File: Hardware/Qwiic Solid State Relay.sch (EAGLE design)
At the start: 42 parts, among them J2 Qwiic Right Angle, J3 Qwiic Right Angle, J9 AVR_SPI_PROG_3X2TESTPOINTS, K1 25A Solid State Relay, K2 25A Solid State Relay, Q1 600mA/40V, Q2 600mA/40V, U4 ATTINY84-ARDUINO

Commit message: post review/checklist changes
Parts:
- added D3, D4: (no value), SparkFun-LED:LED5MM
- added J6: (no value), SparkFun-Connectors:CONN_01PTH_NO_SILK_YES_STOP
- added JP10, JP3, JP8: STAND-OFF, SparkFun-Hardware:STAND-OFF
- added LOGO4: QWIIC_LOGO_5MM, SparkFun-Aesthetics:QWIIC_LOGO_5MM
- added R7, R8: 1k, SparkFun-Resistors:1KOHM-0603-1/10W-1%
- ADR, PWR: value JUMPER-SMT_2_NO_SILK -> JUMPER-SMT_2_NC_TRACE_SILK; device SparkFun-Jumpers:JUMPER-SMT_2_NO_SILK -> SparkFun-Jumpers:JUMPER-SMT_2_NC_TRACE_SILK
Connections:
- removed net N$1: D2.C, Q2.C, R5.1
- removed net N$2: D1.C, Q1.C, R2.1
- removed net RELAY_CTRL3: U4.(A1)1
- removed net RELAY_CTRL4: U4.(A0)0
- new net N$11: D1.C, D3.C, Q1.C, R2.1
- new net N$12: D3.A, R7.1
- new net N$17: D2.C, D4.C, Q2.C, R5.1
- new net N$18: D4.A, R8.1
- net !RESET: now also J6.1
- net 3.3V: now also R7.2, R8.2
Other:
- note added: "VIN: 2.7-5.5V"

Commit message: adding panel
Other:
- note added: "Address 0x6D: HIGH (Open Jumper) Address 0x6C: LOW (Default)"
- note removed: "Address 0x6D: HIGH (Default) Address 0x6C: LOW (Close Jumper)"
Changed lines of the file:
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@@
 <text x="149.86" y="114.3" size="2.54" layer="94" font="vector">ATtiny84</text>
 <text x="63.5" y="114.3" size="2.54" layer="94" font="vector">Programming Header</text>
-<text x="101.6" y="2.54" size="1.27" layer="97" font="vector">Address 0x6D: HIGH (Default)
-Address 0x6C: LOW (Close Jumper)</text>
+<text x="101.6" y="2.54" size="1.27" layer="97" font="vector">Address 0x6D: HIGH (Open Jumper)
+Address 0x6C: LOW (Default)</text>
 <wire x1="119.38" y1="12.7" x2="119.38" y2="7.62" width="0.2032" layer="97" style="dashdot"/>
 <text x="115.824" y="24.638" size="1.27" layer="97" font="vector">Cut jumper

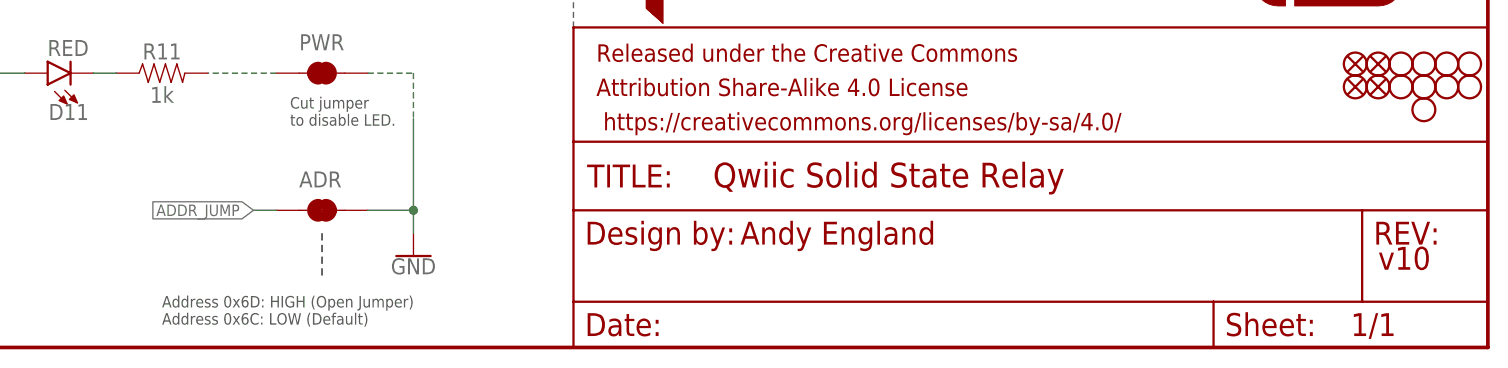
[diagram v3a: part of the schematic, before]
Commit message: updating address note
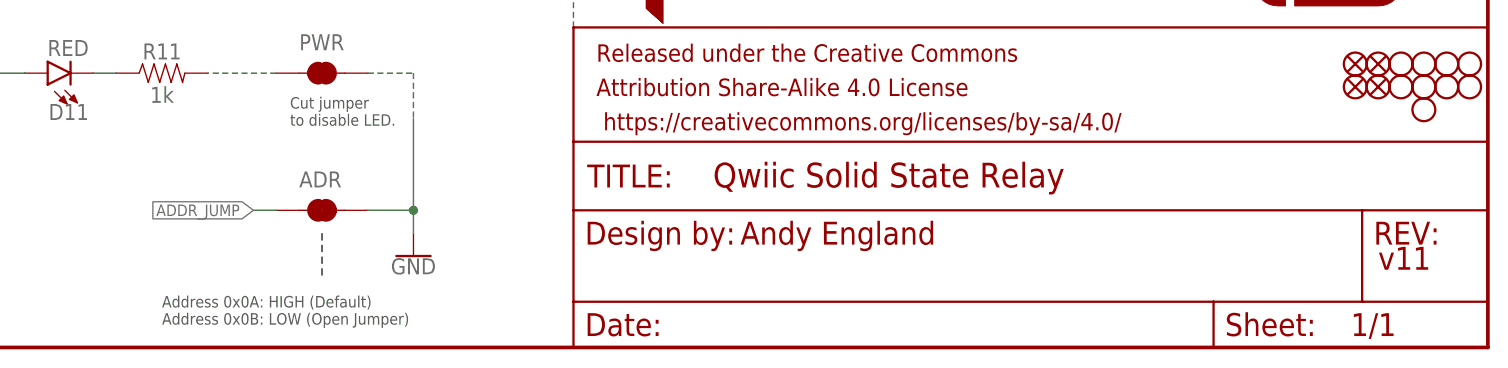
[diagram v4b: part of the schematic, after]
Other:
- note added: "Address 0x0A: HIGH (Default) Address 0x0B: LOW (Open Jumper)"
- note added: "v11"
- note removed: "Address 0x6D: HIGH (Open Jumper) Address 0x6C: LOW (Default)"
- note removed: "v10"
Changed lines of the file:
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@@
 <plain>
 <text x="165.862" y="11.43" size="2.54" layer="94" font="vector">Andy England</text>
-<text x="236.728" y="8.636" size="2.54" layer="94" font="vector">v10</text>
+<text x="236.728" y="8.636" size="2.54" layer="94" font="vector">v11</text>
 <text x="2.54" y="114.3" size="2.54" layer="94" font="vector">Connectors</text>
 <text x="149.86" y="114.3" size="2.54" layer="94" font="vector">ATtiny84</text>
 <text x="63.5" y="114.3" size="2.54" layer="94" font="vector">Programming Header</text>
-<text x="101.6" y="2.54" size="1.27" layer="97" font="vector">Address 0x6D: HIGH (Open Jumper)
-Address 0x6C: LOW (Default)</text>
+<text x="101.6" y="2.54" size="1.27" layer="97" font="vector">Address 0x0A: HIGH (Default)
+Address 0x0B: LOW (Open Jumper)</text>
 <wire x1="119.38" y1="12.7" x2="119.38" y2="7.62" width="0.2032" layer="97" style="dashdot"/>
 <text x="115.824" y="24.638" size="1.27" layer="97" font="vector">Cut jumper
